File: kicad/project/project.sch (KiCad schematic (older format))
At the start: 44 parts, among them J1 SWD, J2 UART, U1 ADS1015, U2 AP7380, U3 STM32L031F4Px, U4 VN7003ALH

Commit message: Components placed
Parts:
- removed BT1: Battery, TerminalBlock:TerminalBlock_bornier-2_P5.08mm, symbol Device:Battery
- removed J2: UART, Connector_PinHeader_2.54mm:PinHeader_1x03_P2.54mm_Vertical, symbol Connector:Conn_01x03_Male
- removed MES1: Voltmeter, Connector_PinHeader_2.54mm:PinHeader_2x01_P2.54mm_Vertical, symbol Device:Voltmeter_DC
- removed MES2: Amperemeter, Connector_PinHeader_2.54mm:PinHeader_2x01_P2.54mm_Vertical, symbol Device:Amperemeter_DC
- added BT1: Battery_Meter, theapi:TerminalBlock_Meter, symbol theapi_Battery:Battery_Meter
- added J3: Voltmeter, Connector_PinHeader_2.54mm:PinHeader_1x02_P2.54mm_Vertical_SMD_Pin1Left, symbol Connector:Conn_01x02_Male
- TP1: footprint TestPoint:TestPoint_Pad_2.0x2.0mm -> TestPoint:TestPoint_Pad_D1.0mm
- U4: footprint Package_TO_SOT_SMD:Infineon_PG-TO-220-7Lead_TabPin8 -> theapi:Octapak
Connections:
- net labels added: -BATT
- net labels removed: UART_RX
- wire segments 94 -> 101
- no-connect marks 0 -> 1
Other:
- note removed: "UART Header"
- moved on the sheet: D4, D5, R17
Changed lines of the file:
@@
 Text GLabel 4550 4025 2    50   Input ~ 0
 UART_TX
-Text GLabel 4550 4125 2    50   Input ~ 0
-UART_RX
 Text GLabel 3550 3825 0    50   Input ~ 0
 NRST
@@
 $EndComp
 Wire Wire Line
-	8750 4575 9200 4575
-Wire Wire Line
-	8750 4475 9200 4475
-Wire Wire Line
-	9200 4475 9200 4575
-Connection ~ 9200 4575
-Wire Wire Line
-	8750 4675 8975 4675
-Wire Wire Line
-	9200 4675 9200 4575
+	8750 4475 8900 4475
 $Comp
 L power:GND #PWR035
 U 1 1 5C7B5C1D
-P 10425 5375
-F 0 "#PWR035" H 10425 5125 50  0001 C CNN
-F 1 "GND" H 10430 5202 50  0000 C CNN
-F 2 "" H 10425 5375 50  0001 C CNN
-F 3 "" H 10425 5375 50  0001 C CNN
-	1    10425 5375
+P 10150 5150
+F 0 "#PWR035" H 10150 4900 50  0001 C CNN
+F 1 "GND" H 10155 4977 50  0000 C CNN
+F 2 "" H 10150 5150 50  0001 C CNN
+F 3 "" H 10150 5150 50  0001 C CNN
+	1    10150 5150
 	1    0    0    -1
 $EndComp
@@
 L Device:R R17
 U 1 1 5C7C0432
-P 8975 5075
-F 0 "R17" H 9045 5121 50  0000 L CNN
-F 1 "10K" H 9045 5030 50  0000 L CNN
-F 2 "Resistor_SMD:R_0603_1608Metric_Pad1.05x0.95mm_HandSolder" V 8905 5075 50  0001 C CNN
-F 3 "~" H 8975 5075 50  0001 C CNN
-	1    8975 5075
+P 9150 4850
+F 0 "R17" H 9220 4896 50  0000 L CNN
+F 1 "10K" H 9220 4805 50  0000 L CNN
+F 2 "Resistor_SMD:R_0603_1608Metric_Pad1.05x0.95mm_HandSolder" V 9080 4850 50  0001 C CNN
+F 3 "~" H 9150 4850 50  0001 C CNN
+	1    9150 4850
 	1    0    0    -1
 $EndComp
@@
 L Device:LED D4
 U 1 1 5C7C051B
-P 8975 5525
-F 0 "D4" V 9013 5408 50  0000 R CNN
-F 1 "LED" V 8922 5408 50  0000 R CNN
-F 2 "LED_SMD:LED_0805_2012Metric_Pad1.15x1.40mm_HandSolder" H 8975 5525 50  0001 C CNN
-F 3 "~" H 8975 5525 50  0001 C CNN
-	1    8975 5525
+P 9150 5300
+F 0 "D4" V 9188 5183 50  0000 R CNN
+F 1 "LED" V 9097 5183 50  0000 R CNN
+F 2 "LED_SMD:LED_0805_2012Metric_Pad1.15x1.40mm_HandSolder" H 9150 5300 50  0001 C CNN
+F 3 "~" H 9150 5300 50  0001 C CNN
+	1    9150 5300
 	0    -1   -1   0
 $EndComp
@@
 L power:GND #PWR032
 U 1 1 5C7C05D8
-P 8975 5675
-F 0 "#PWR032" H 8975 5425 50  0001 C CNN
-F 1 "GND" H 8980 5502 50  0000 C CNN
-F 2 "" H 8975 5675 50  0001 C CNN
-F 3 "" H 8975 5675 50  0001 C CNN
-	1    8975 5675
-	1    0    0    -1
-$EndComp
-Wire Wire Line
-	8975 5375 8975 5225
-Wire Wire Line
-	8975 4925 8975 4675
-Connection ~ 8975 4675
-Wire Wire Line
-	8975 4675 9200 4675
+P 9150 5450
+F 0 "#PWR032" H 9150 5200 50  0001 C CNN
+F 1 "GND" H 9155 5277 50  0000 C CNN
+F 2 "" H 9150 5450 50  0001 C CNN
+F 3 "" H 9150 5450 50  0001 C CNN
+	1    9150 5450
+	1    0    0    -1
+$EndComp
+Wire Wire Line
+	9150 5150 9150 5000
 $Comp
 L Device:LED D1
@@
 $EndComp
 Wire Wire Line
-	10425 4575 10425 2675
-Wire Wire Line
 	6900 3175 7125 3175
 Text Label 6375 3925 0    50   ~ 0
@@
 Wire Wire Line
 	3550 4025 3150 4025
-$Comp
-L Connector:Conn_01x03_Male J2
-U 1 1 5C7BD41A
-P 9250 1475
-F 0 "J2" H 9222 1405 50  0000 R CNN
-F 1 "UART" H 9222 1496 50  0000 R CNN
-F 2 "Connector_PinHeader_2.54mm:PinHeader_1x03_P2.54mm_Vertical" H 9250 1475 50  0001 C CNN
-F 3 "~" H 9250 1475 50  0001 C CNN
-	1    9250 1475
-	1    0    0    1
-$EndComp
-$Comp
-L power:GND #PWR034
-U 1 1 5C7BEAD9
-P 9450 1575
-F 0 "#PWR034" H 9450 1325 50  0001 C CNN
-F 1 "GND" H 9455 1402 50  0000 C CNN
-F 2 "" H 9450 1575 50  0001 C CNN
-F 3 "" H 9450 1575 50  0001 C CNN
-	1    9450 1575
-	1    0    0    -1
-$EndComp
-Text GLabel 9450 1475 2    50   Input ~ 0
-UART_TX
-Text GLabel 9450 1375 2    50   Input ~ 0
-UART_RX
 $Comp
 L power:+3V3 #PWR024
@@
 F 0 "TP1" V 1400 7475 50  0000 L CNN
 F 1 "TestPoint" V 1400 7475 50  0001 L CNN
-F 2 "TestPoint:TestPoint_Pad_2.0x2.0mm" H 1600 7275 50  0001 C CNN
+F 2 "TestPoint:TestPoint_Pad_D1.0mm" H 1600 7275 50  0001 C CNN
 F 3 "~" H 1600 7275 50  0001 C CNN
 	1    1400 7275
@@
 	1    0    0    -1
 $EndComp
-$Comp
-L Device:Battery BT1
-U 1 1 5C80B97F
-P 10425 5175
-F 0 "BT1" H 10533 5221 50  0000 L CNN
-F 1 "Battery" H 10533 5130 50  0000 L CNN
-F 2 "TerminalBlock:TerminalBlock_bornier-2_P5.08mm" V 10425 5235 50  0001 C CNN
-F 3 "~" V 10425 5235 50  0001 C CNN
-	1    10425 5175
-	1    0    0    -1
-$EndComp
 Wire Notes Line
 	4700 600  7900 600
@@
 Wire Notes Line
 	4700 2350 4700 625
-Wire Notes Line
-	7950 600  7950 2350
-Wire Notes Line
-	7975 2350 11025 2350
-Wire Notes Line
-	11025 2350 11025 600
-Wire Notes Line
-	11025 600  7950 600
 Text Notes 4775 800  0    98   ~ 20
 SWD Header
-Text Notes 8025 800  0    98   ~ 20
-UART Header
 Wire Wire Line
 	2475 4725 2150 4725
@@
 L Device:D_Schottky D5
 U 1 1 5C7C7D61
-P 9475 4575
-F 0 "D5" H 9475 4359 50  0000 C CNN
-F 1 "D_Schottky" H 9475 4450 50  0000 C CNN
-F 2 "Diode_THT:D_5KP_P10.16mm_Horizontal" H 9475 4575 50  0001 C CNN
-F 3 "~" H 9475 4575 50  0001 C CNN
-	1    9475 4575
+P 9475 4475
+F 0 "D5" H 9475 4259 50  0000 C CNN
+F 1 "D_Schottky" H 9475 4350 50  0000 C CNN
+F 2 "Diode_THT:D_5KP_P10.16mm_Horizontal" H 9475 4475 50  0001 C CNN
+F 3 "~" H 9475 4475 50  0001 C CNN
+	1    9475 4475
 	-1   0    0    1
 $EndComp
@@
 F 0 "U4" H 8375 4475 50  0000 C CNN
 F 1 "VN7003ALH" H 8550 3600 50  0000 C CNN
-F 2 "Package_TO_SOT_SMD:Infineon_PG-TO-220-7Lead_TabPin8" H 8300 4225 50  0001 C CNN
+F 2 "theapi:Octapak" H 8300 4225 50  0001 C CNN
 F 3 "" H 8300 4225 50  0001 C CNN
 	1    8300 4225
@@
 Wire Wire Line
 	1700 1000 2050 1000
-$Comp
-L Device:Amperemeter_DC MES2
-U 1 1 5C82C864
-P 10425 4775
-F 0 "MES2" H 10300 4850 50  0000 R CNN
-F 1 "Amperemeter" H 10375 4950 50  0000 R CNN
-F 2 "Connector_PinHeader_2.54mm:PinHeader_2x01_P2.54mm_Vertical" V 10425 4875 50  0001 C CNN
-F 3 "~" V 10425 4875 50  0001 C CNN
-	1    10425 4775
+Wire Wire Line
+	7500 2675 7600 2675
+$Comp
+L Connector:Conn_01x02_Male J3
+U 1 1 5C83132D
+P 10025 4225
+F 0 "J3" H 9997 4105 50  0000 R CNN
+F 1 "Voltmeter" H 10225 4025 50  0000 R CNN
+F 2 "Connector_PinHeader_2.54mm:PinHeader_1x02_P2.54mm_Vertical_SMD_Pin1Left" H 10025 4225 50  0001 C CNN
+F 3 "~" H 10025 4225 50  0001 C CNN
+	1    10025 4225
 	-1   0    0    1
 $EndComp
-Connection ~ 10425 4575
-$Comp
-L Device:Voltmeter_DC MES1
-U 1 1 5C83B4FA
-P 9725 4775
-F 0 "MES1" H 9850 4700 50  0000 L CNN
-F 1 "Voltmeter" H 9775 4600 50  0000 L CNN
-F 2 "Connector_PinHeader_2.54mm:PinHeader_2x01_P2.54mm_Vertical" V 9725 4875 50  0001 C CNN
-F 3 "~" V 9725 4875 50  0001 C CNN
-	1    9725 4775
-	1    0    0    -1
-$EndComp
-Wire Wire Line
-	9725 4575 10425 4575
-$Comp
-L power:GND #PWR036
-U 1 1 5C8412BA
-P 9725 4975
-F 0 "#PWR036" H 9725 4725 50  0001 C CNN
-F 1 "GND" H 9730 4802 50  0000 C CNN
-F 2 "" H 9725 4975 50  0001 C CNN
-F 3 "" H 9725 4975 50  0001 C CNN
-	1    9725 4975
-	1    0    0    -1
-$EndComp
-Wire Wire Line
-	9200 4575 9325 4575
-Wire Wire Line
-	9625 4575 9725 4575
-Connection ~ 9725 4575
-Wire Wire Line
-	7600 2675 10425 2675
+$Comp
+L power:+24V #PWR036
+U 1 1 5C83171F
+P 9775 4025
+F 0 "#PWR036" H 9775 3875 50  0001 C CNN
+F 1 "+24V" H 9790 4198 50  0000 C CNN
+F 2 "" H 9775 4025 50  0001 C CNN
+F 3 "" H 9775 4025 50  0001 C CNN
+	1    9775 4025
+	1    0    0    -1
+$EndComp
+Wire Wire Line
+	9775 4025 9775 4125
+Wire Wire Line
+	9775 4125 9825 4125
+Wire Wire Line
+	9825 4225 9825 4475
+Connection ~ 9825 4475
+Connection ~ 10325 4475
+Wire Wire Line
+	10325 4475 10325 2675
+Wire Wire Line
+	10325 4475 10325 4675
+Wire Wire Line
+	8750 4575 8900 4575
+Wire Wire Line
+	8900 4575 8900 4475
+Wire Wire Line
+	8750 4675 8900 4675
+Wire Wire Line
+	8900 4675 8900 4575
+Connection ~ 8900 4575
+Wire Wire Line
+	8900 4475 9150 4475
+Connection ~ 8900 4475
+Wire Wire Line
+	9150 4700 9150 4475
+Connection ~ 9150 4475
+Wire Wire Line
+	9150 4475 9325 4475
+NoConn ~ 4550 4125
+$Comp
+L theapi_Battery:Battery_Meter BT1
+U 1 1 5C87CDCA
+P 10425 4875
+F 0 "BT1" H 10200 4950 50  0000 L CNN
+F 1 "Battery_Meter" H 9850 4875 50  0000 L CNN
+F 2 "theapi:TerminalBlock_Meter" H 10425 4875 50  0001 C CNN
+F 3 "" H 10425 4875 50  0001 C CNN
+	1    10425 4875
+	1    0    0    -1
+$EndComp
+Wire Wire Line
+	10150 5150 10150 5125
+Wire Wire Line
+	10150 5125 10325 5125
+$Comp
+L power:-BATT #PWR0101
+U 1 1 5C892492
+P 10525 5825
+F 0 "#PWR0101" H 10525 5675 50  0001 C CNN
+F 1 "-BATT" H 10540 5998 50  0000 C CNN
+F 2 "" H 10525 5825 50  0001 C CNN
+F 3 "" H 10525 5825 50  0001 C CNN
+	1    10525 5825
+	-1   0    0    1
+$EndComp
+Connection ~ 7600 2675
+Wire Wire Line
+	7600 2675 10325 2675
+Wire Wire Line
+	9825 4475 10325 4475
+Wire Wire Line
+	9625 4475 9825 4475
 $EndSCHEMATC

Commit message: Main power traces
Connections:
- net FR_DIAG: now also R12.1, U4.6 (FR_DIAG); no longer R12.2, U3.12 (PA6)
- net INPUT: now reaches R11.1, U4.4 (INPUT)
- net OUT: now reaches D5.2 (A), R17.1, U4.1 (OUTPUT), U4.2 (OUTPUT), U4.3 (OUTPUT)
- new net: R12.2, U3.12 (PA6)
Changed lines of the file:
@@
 Wire Wire Line
 	4550 4425 7000 4425
-Text Label 5025 4425 0    50   ~ 0
+Text Label 7550 4425 0    50   ~ 0
 FR_DIAG
 Text Label 5025 4325 0    50   ~ 0
@@
 Wire Wire Line
 	1700 1000 2050 1000
-Wire Wire Line
-	7500 2675 7600 2675
 $Comp
 L Connector:Conn_01x02_Male J3
@@
 	-1   0    0    1
 $EndComp
-Connection ~ 7600 2675
 Wire Wire Line
 	7600 2675 10325 2675
@@
 Wire Wire Line
 	9625 4475 9825 4475
+Text Label 9200 4475 0    50   ~ 0
+OUT
+Text Label 7550 4325 0    50   ~ 0
+INPUT
 $EndSCHEMATC

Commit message: Connections
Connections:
- net LED_2: now reaches R2.2, U3.3 (PC15)
- net LED renamed LED_1
- net OUT renamed LED_4
- net PA4 renamed LED_3
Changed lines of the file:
@@
 Wire Wire Line
 	7700 4575 7950 4575
-Text Label 5025 4225 0    50   ~ 0
-PA4
 Wire Wire Line
 	4550 4325 7000 4325
@@
 	0    -1   -1   0
 $EndComp
-Text Label 3400 4625 0    50   ~ 0
-LED
+Text Label 2825 4625 0    50   ~ 0
+LED_1
 $Comp
 L Device:R R15
@@
 Text Label 7550 4325 0    50   ~ 0
 INPUT
+Text Label 2825 4725 0    50   ~ 0
+LED_2
+Text Label 5025 4225 0    50   ~ 0
+LED_3
+Text Label 9150 4625 0    50   ~ 0
+LED_4
 $EndSCHEMATC

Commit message: Tidying
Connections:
- net Earth is gone; now on net GND: C2.2
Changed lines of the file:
@@
-$EndComp
-$Comp
-L power:Earth #PWR09
-U 1 1 593024E3
-P 3150 6425
-F 0 "#PWR09" H 3150 6175 50  0001 C CNN
-F 1 "Earth" H 3150 6275 50  0001 C CNN
-F 2 "" H 3150 6425 50  0000 C CNN
-F 3 "" H 3150 6425 50  0000 C CNN
-	1    3150 6425
-	-1   0    0    -1
 $EndComp
 $Comp
@@
 Text Label 9150 4625 0    50   ~ 0
 LED_4
+$Comp
+L power:GND #PWR?
+U 1 1 5C843977
+P 3150 6425
+F 0 "#PWR?" H 3150 6175 50  0001 C CNN
+F 1 "GND" H 3155 6252 50  0000 C CNN
+F 2 "" H 3150 6425 50  0001 C CNN
+F 3 "" H 3150 6425 50  0001 C CNN
+	1    3150 6425
+	1    0    0    -1
+$EndComp
 $EndSCHEMATC

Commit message: Changed diode footprint
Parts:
- D5: footprint Diode_THT:D_5KP_P10.16mm_Horizontal -> Diode_THT:D_DO-201AD_P12.70mm_Horizontal
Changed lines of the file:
@@
 	0    1    1    0
 $EndComp
-Wire Wire Line
-	7300 4325 7950 4325
 $Comp
 L Device:R R13
@@
 F 0 "D5" H 9475 4259 50  0000 C CNN
 F 1 "D_Schottky" H 9475 4350 50  0000 C CNN
-F 2 "Diode_THT:D_5KP_P10.16mm_Horizontal" H 9475 4475 50  0001 C CNN
+F 2 "Diode_THT:D_DO-201AD_P12.70mm_Horizontal" H 9475 4475 50  0001 C CNN
 F 3 "~" H 9475 4475 50  0001 C CNN
 	1    9475 4475
@@
 LED_4
 $Comp
-L power:GND #PWR?
+L power:GND #PWR0102
 U 1 1 5C843977
 P 3150 6425
-F 0 "#PWR?" H 3150 6175 50  0001 C CNN
+F 0 "#PWR0102" H 3150 6175 50  0001 C CNN
 F 1 "GND" H 3155 6252 50  0000 C CNN
 F 2 "" H 3150 6425 50  0001 C CNN
@@
 	1    0    0    -1
 $EndComp
+Wire Wire Line
+	7300 4325 7950 4325
 $EndSCHEMATC

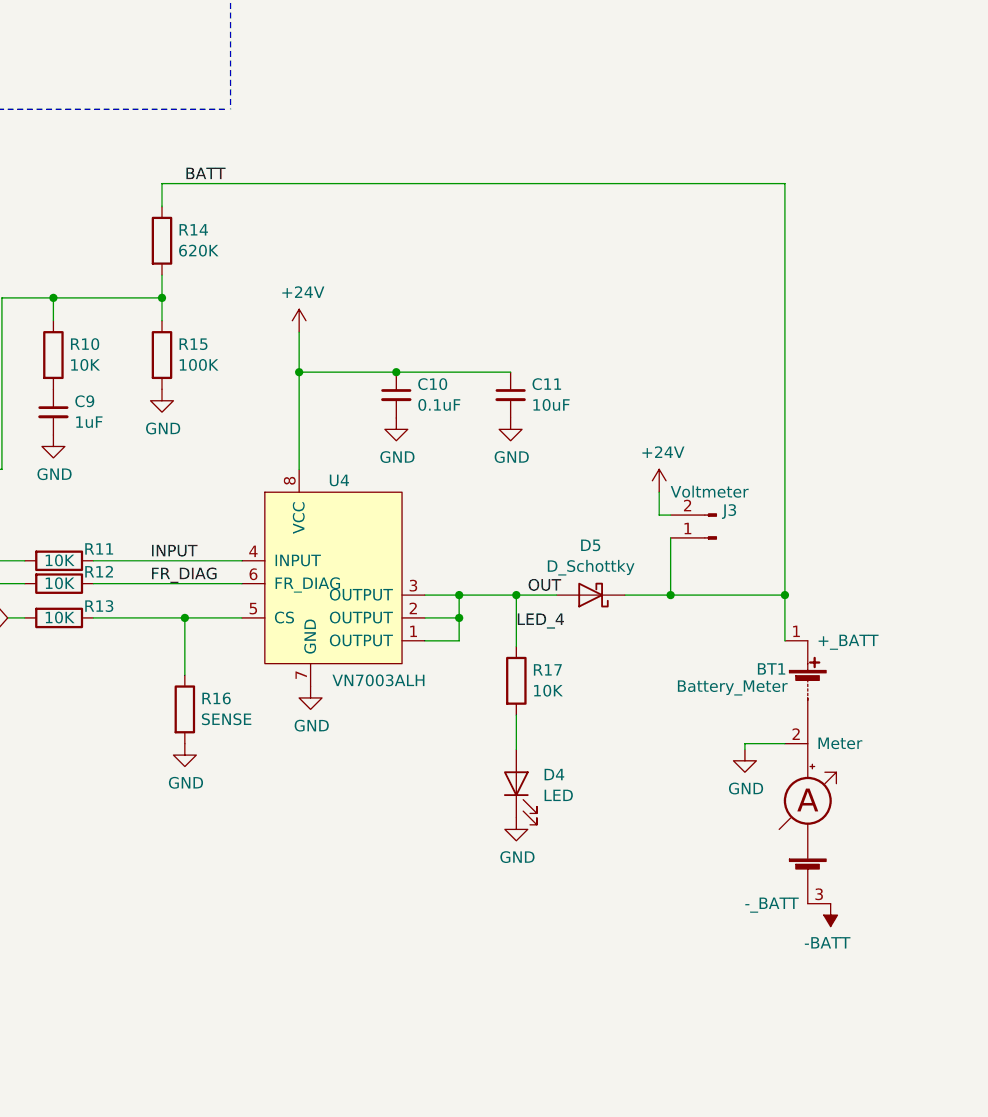
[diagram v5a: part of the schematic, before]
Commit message: Sense battery before the diode
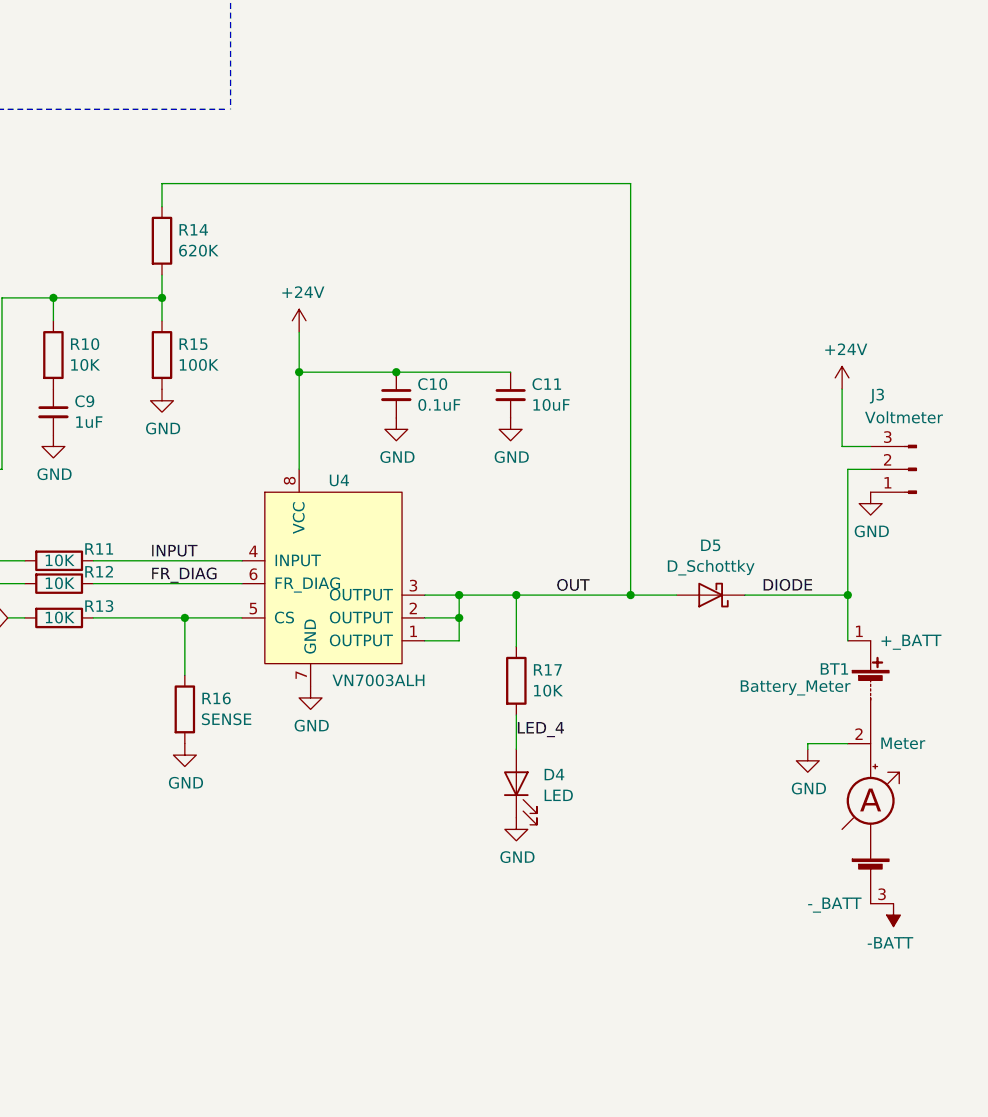
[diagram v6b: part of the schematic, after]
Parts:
- removed J3: Voltmeter, Connector_PinHeader_2.54mm:PinHeader_1x02_P2.54mm_Vertical_SMD_Pin1Left, symbol Connector:Conn_01x02_Male
- added J3: Voltmeter, Connector_PinHeader_2.54mm:PinHeader_1x03_P2.54mm_Vertical_SMD_Pin1Right, symbol Connector:Conn_01x03_Male
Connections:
- net +24V: now also J3.3 (Pin_3)
- net GND: now also J3.1 (Pin_1)
- net LED_4: now also D4.2 (A), R17.2; no longer D5.2 (A), R17.1, U4.1 (OUTPUT), U4.2 (OUTPUT), U4.3 (OUTPUT)
- net BATT renamed DIODE
- net DIODE: now also J3.2 (Pin_2); no longer R14.1
- new net OUT: D5.2 (A), R14.1, R17.1, U4.1 (OUTPUT), U4.2 (OUTPUT), U4.3 (OUTPUT)
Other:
- moved on the sheet: BT1, D5
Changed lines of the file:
@@
 L power:GND #PWR035
 U 1 1 5C7B5C1D
-P 10150 5150
-F 0 "#PWR035" H 10150 4900 50  0001 C CNN
-F 1 "GND" H 10155 4977 50  0000 C CNN
-F 2 "" H 10150 5150 50  0001 C CNN
-F 3 "" H 10150 5150 50  0001 C CNN
-	1    10150 5150
+P 10425 5150
+F 0 "#PWR035" H 10425 4900 50  0001 C CNN
+F 1 "GND" H 10430 4977 50  0000 C CNN
+F 2 "" H 10425 5150 50  0001 C CNN
+F 3 "" H 10425 5150 50  0001 C CNN
+	1    10425 5150
 	1    0    0    -1
 $EndComp
@@
 Wire Wire Line
 	7600 2675 7600 2775
-Text Label 7700 2675 0    50   ~ 0
-BATT
 Wire Wire Line
 	7300 4425 7950 4425
@@
 L Device:D_Schottky D5
 U 1 1 5C7C7D61
-P 9475 4475
-F 0 "D5" H 9475 4259 50  0000 C CNN
-F 1 "D_Schottky" H 9475 4350 50  0000 C CNN
-F 2 "Diode_THT:D_DO-201AD_P12.70mm_Horizontal" H 9475 4475 50  0001 C CNN
-F 3 "~" H 9475 4475 50  0001 C CNN
-	1    9475 4475
+P 10000 4475
+F 0 "D5" H 10000 4259 50  0000 C CNN
+F 1 "D_Schottky" H 10000 4350 50  0000 C CNN
+F 2 "Diode_THT:D_DO-201AD_P12.70mm_Horizontal" H 10000 4475 50  0001 C CNN
+F 3 "~" H 10000 4475 50  0001 C CNN
+	1    10000 4475
 	-1   0    0    1
 $EndComp
@@
 	1700 1000 2050 1000
 $Comp
-L Connector:Conn_01x02_Male J3
-U 1 1 5C83132D
-P 10025 4225
-F 0 "J3" H 9997 4105 50  0000 R CNN
-F 1 "Voltmeter" H 10225 4025 50  0000 R CNN
-F 2 "Connector_PinHeader_2.54mm:PinHeader_1x02_P2.54mm_Vertical_SMD_Pin1Left" H 10025 4225 50  0001 C CNN
-F 3 "~" H 10025 4225 50  0001 C CNN
-	1    10025 4225
-	-1   0    0    1
-$EndComp
-$Comp
 L power:+24V #PWR036
 U 1 1 5C83171F
-P 9775 4025
-F 0 "#PWR036" H 9775 3875 50  0001 C CNN
-F 1 "+24V" H 9790 4198 50  0000 C CNN
-F 2 "" H 9775 4025 50  0001 C CNN
-F 3 "" H 9775 4025 50  0001 C CNN
-	1    9775 4025
-	1    0    0    -1
-$EndComp
-Wire Wire Line
-	9775 4025 9775 4125
-Wire Wire Line
-	9775 4125 9825 4125
-Wire Wire Line
-	9825 4225 9825 4475
-Connection ~ 9825 4475
-Connection ~ 10325 4475
-Wire Wire Line
-	10325 4475 10325 2675
-Wire Wire Line
-	10325 4475 10325 4675
+P 10575 3575
+F 0 "#PWR036" H 10575 3425 50  0001 C CNN
+F 1 "+24V" H 10590 3748 50  0000 C CNN
+F 2 "" H 10575 3575 50  0001 C CNN
+F 3 "" H 10575 3575 50  0001 C CNN
+	1    10575 3575
+	1    0    0    -1
+$EndComp
+Wire Wire Line
+	10600 4475 10600 4675
 Wire Wire Line
 	8750 4575 8900 4575
@@
 Connection ~ 9150 4475
 Wire Wire Line
-	9150 4475 9325 4475
+	9150 4475 9650 4475
 NoConn ~ 4550 4125
 $Comp
 L theapi_Battery:Battery_Meter BT1
 U 1 1 5C87CDCA
-P 10425 4875
-F 0 "BT1" H 10200 4950 50  0000 L CNN
-F 1 "Battery_Meter" H 9850 4875 50  0000 L CNN
-F 2 "theapi:TerminalBlock_Meter" H 10425 4875 50  0001 C CNN
-F 3 "" H 10425 4875 50  0001 C CNN
-	1    10425 4875
-	1    0    0    -1
-$EndComp
-Wire Wire Line
-	10150 5150 10150 5125
-Wire Wire Line
-	10150 5125 10325 5125
+P 10700 4875
+F 0 "BT1" H 10475 4950 50  0000 L CNN
+F 1 "Battery_Meter" H 10125 4875 50  0000 L CNN
+F 2 "theapi:TerminalBlock_Meter" H 10700 4875 50  0001 C CNN
+F 3 "" H 10700 4875 50  0001 C CNN
+	1    10700 4875
+	1    0    0    -1
+$EndComp
+Wire Wire Line
+	10425 5150 10425 5125
+Wire Wire Line
+	10425 5125 10600 5125
 $Comp
 L power:-BATT #PWR0101
 U 1 1 5C892492
-P 10525 5825
-F 0 "#PWR0101" H 10525 5675 50  0001 C CNN
-F 1 "-BATT" H 10540 5998 50  0000 C CNN
-F 2 "" H 10525 5825 50  0001 C CNN
-F 3 "" H 10525 5825 50  0001 C CNN
-	1    10525 5825
+P 10800 5825
+F 0 "#PWR0101" H 10800 5675 50  0001 C CNN
+F 1 "-BATT" H 10815 5998 50  0000 C CNN
+F 2 "" H 10800 5825 50  0001 C CNN
+F 3 "" H 10800 5825 50  0001 C CNN
+	1    10800 5825
 	-1   0    0    1
 $EndComp
 Wire Wire Line
-	7600 2675 10325 2675
-Wire Wire Line
-	9825 4475 10325 4475
-Wire Wire Line
-	9625 4475 9825 4475
-Text Label 9200 4475 0    50   ~ 0
+	7600 2675 9650 2675
+Text Label 9325 4475 0    50   ~ 0
 OUT
 Text Label 7550 4325 0    50   ~ 0
@@
 Text Label 5025 4225 0    50   ~ 0
 LED_3
-Text Label 9150 4625 0    50   ~ 0
+Text Label 9150 5100 0    50   ~ 0
 LED_4
 $Comp
@@
 Wire Wire Line
 	7300 4325 7950 4325
+Connection ~ 9650 4475
+Wire Wire Line
+	9650 4475 9850 4475
+Connection ~ 10600 4475
+Wire Wire Line
+	9650 2675 9650 4475
+Wire Wire Line
+	10150 4475 10600 4475
+Text Label 10225 4475 0    50   ~ 0
+DIODE
+$Comp
+L Connector:Conn_01x03_Male J3
+U 1 1 5C8760FB
+P 10900 3925
+F 0 "J3" H 11100 3600 50  0000 R CNN
+F 1 "Voltmeter" H 11125 3700 50  0000 R CNN
+F 2 "Connector_PinHeader_2.54mm:PinHeader_1x03_P2.54mm_Vertical_SMD_Pin1Right" H 10900 3925 50  0001 C CNN
+F 3 "~" H 10900 3925 50  0001 C CNN
+	1    10900 3925
+	-1   0    0    1
+$EndComp
+Wire Wire Line
+	10575 3575 10575 3825
+Wire Wire Line
+	10575 3825 10700 3825
+Wire Wire Line
+	10600 3925 10700 3925
+Wire Wire Line
+	10600 3925 10600 4475
+$Comp
+L power:GND #PWR09
+U 1 1 5C881C03
+P 10700 4025
+F 0 "#PWR09" H 10700 3775 50  0001 C CNN
+F 1 "GND" H 10705 3852 50  0000 C CNN
+F 2 "" H 10700 4025 50  0001 C CNN
+F 3 "" H 10700 4025 50  0001 C CNN
+	1    10700 4025
+	1    0    0    -1
+$EndComp
 $EndSCHEMATC

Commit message: Voltmeter header
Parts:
- J3: footprint Connector_PinHeader_2.54mm:PinHeader_1x03_P2.54mm_Vertical_SMD_Pin1Right -> theapi:Voltmeter_Header_1x03
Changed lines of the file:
@@
 F 0 "J3" H 11100 3600 50  0000 R CNN
 F 1 "Voltmeter" H 11125 3700 50  0000 R CNN
-F 2 "Connector_PinHeader_2.54mm:PinHeader_1x03_P2.54mm_Vertical_SMD_Pin1Right" H 10900 3925 50  0001 C CNN
+F 2 "theapi:Voltmeter_Header_1x03" H 10900 3925 50  0001 C CNN
 F 3 "~" H 10900 3925 50  0001 C CNN
 	1    10900 3925
